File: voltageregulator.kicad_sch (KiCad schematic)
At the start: 38 parts, among them Q1 Si2319CDS, U1 LM317_SOT-223, U2 LM337_SOT223, U3 TPS65131RGE

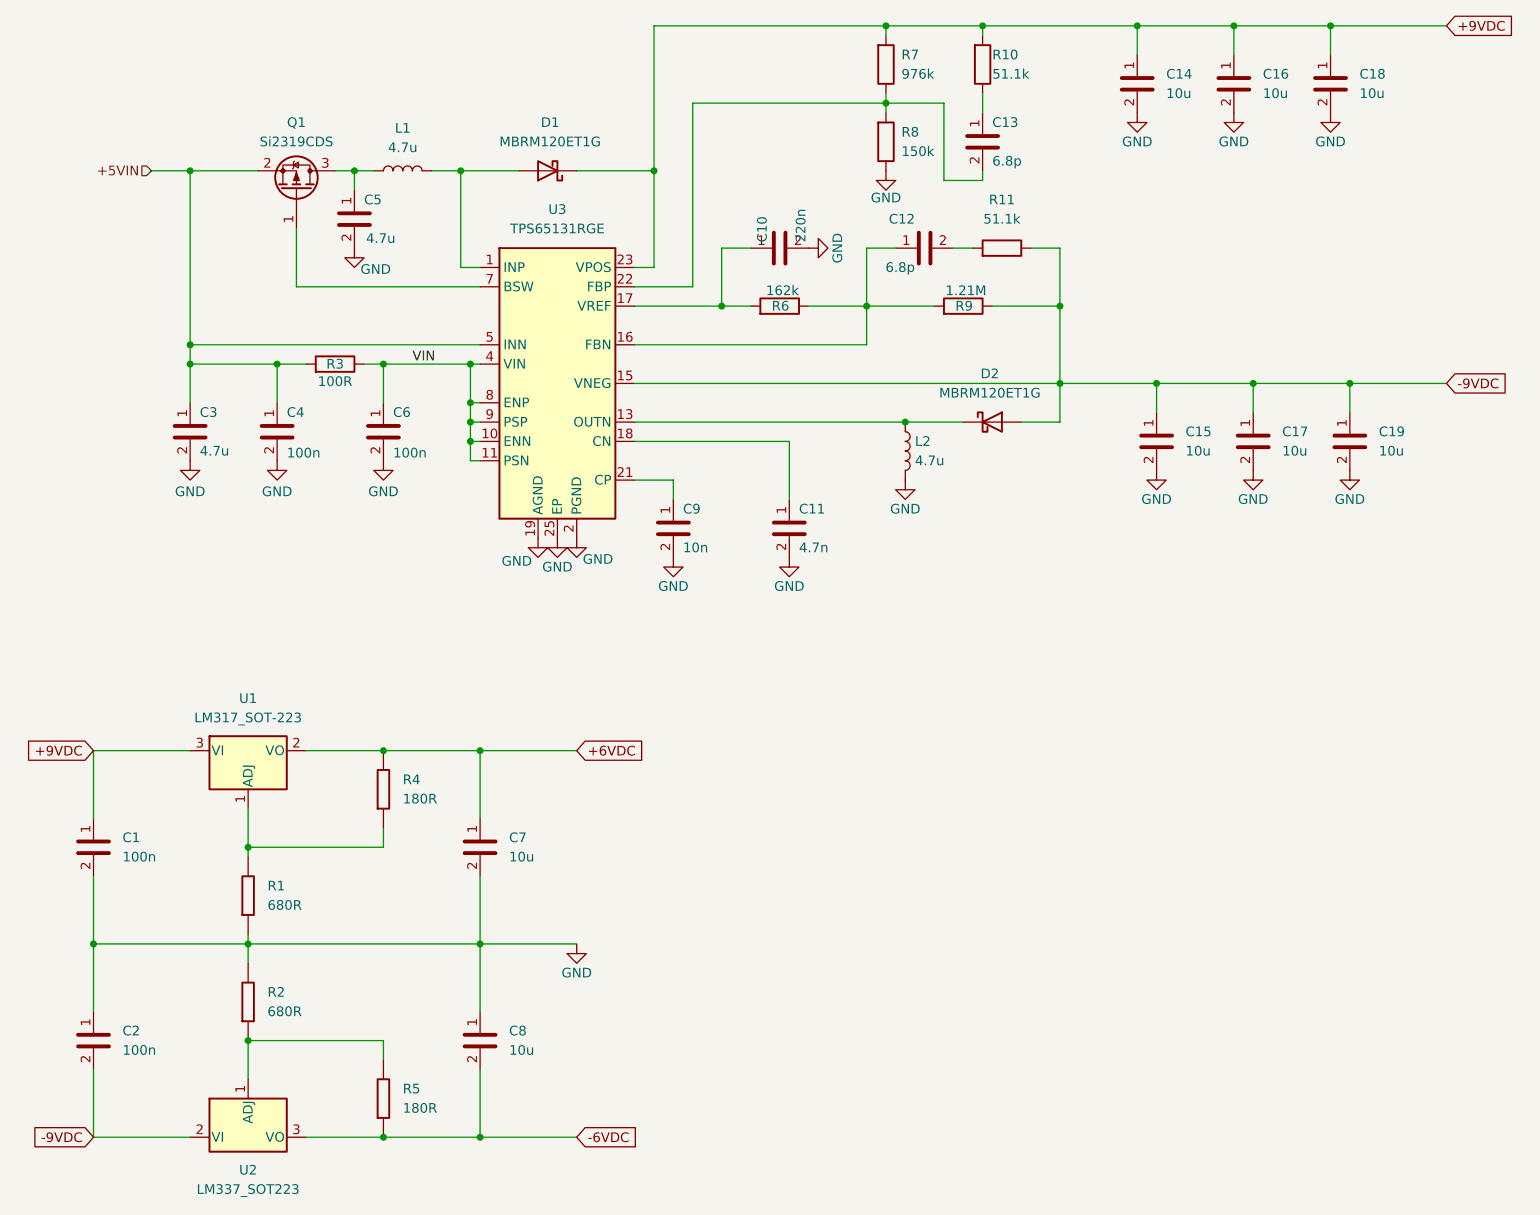
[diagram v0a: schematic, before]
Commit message: Added photodiode circuit.
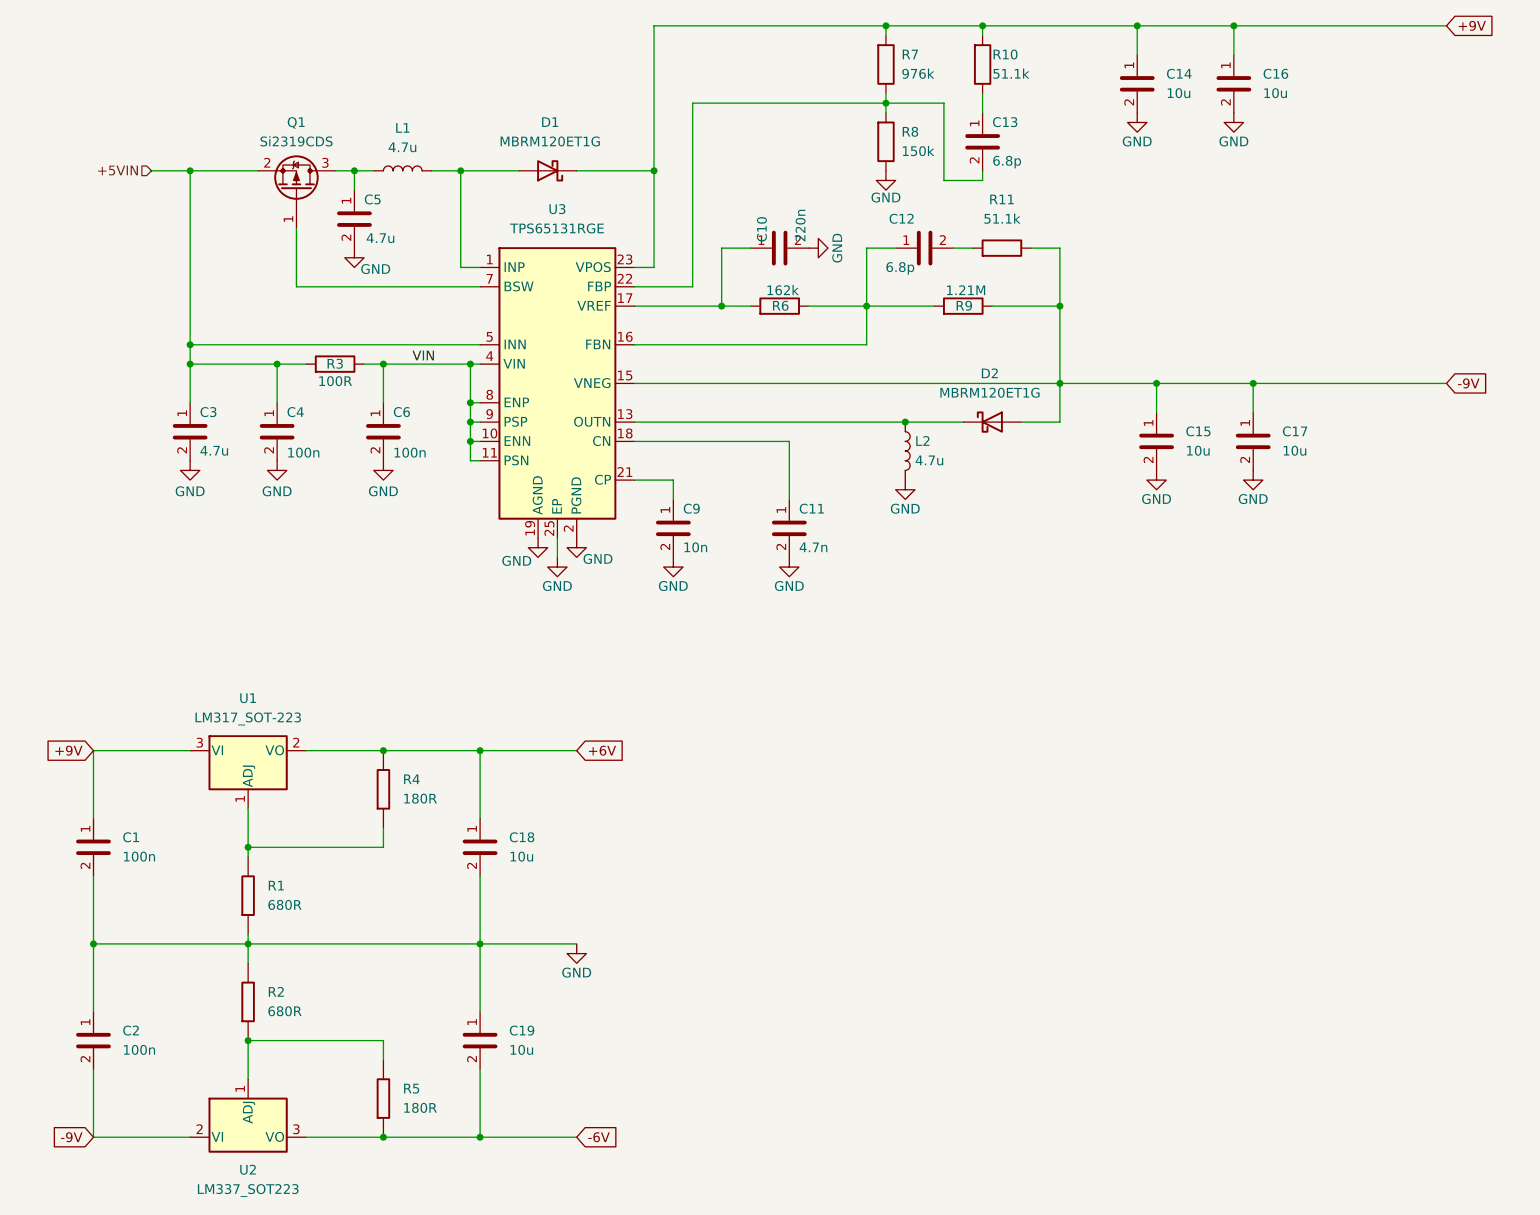
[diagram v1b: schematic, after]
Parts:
- removed C7, C8: 10u, Capacitor_SMD:C_0603_1608Metric_Pad1.08x0.95mm_HandSolder, symbol 1_C_SMD:C_0603_10u
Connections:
- net GND: now also C19.1; no longer C19.2
- net +6VDC renamed +6V
- net +6V: now also C18.1
- net +9VDC renamed +9V
- net +9V: no longer C18.1
- net -6VDC renamed -6V
- net -6V: now also C19.2
- net -9VDC renamed -9V
- net -9V: no longer C19.1

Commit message: Update schematic and pcb. Add fab files.
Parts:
- D1, D2: Package/Footprint (none) -> DO-216AA; Type (none) -> SMD
- L1, L2: Type (none) -> SMD
- Q1: Package/Footprint (none) -> SOT-23
- R1, R2, R4, R5: Package/Footprint (none) -> 0603
- R10, R11, R3, R6, R7, R8, R9: Package/Footprint (none) -> 0402
